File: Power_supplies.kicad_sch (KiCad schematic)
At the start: 59 parts, among them J2 DG35C-B-02P, T1 AOSP21357, T2 MJD32C, U3 MC34063, U31 AP331A, U4 MC34063, U5 TLV70233_SOT23-5

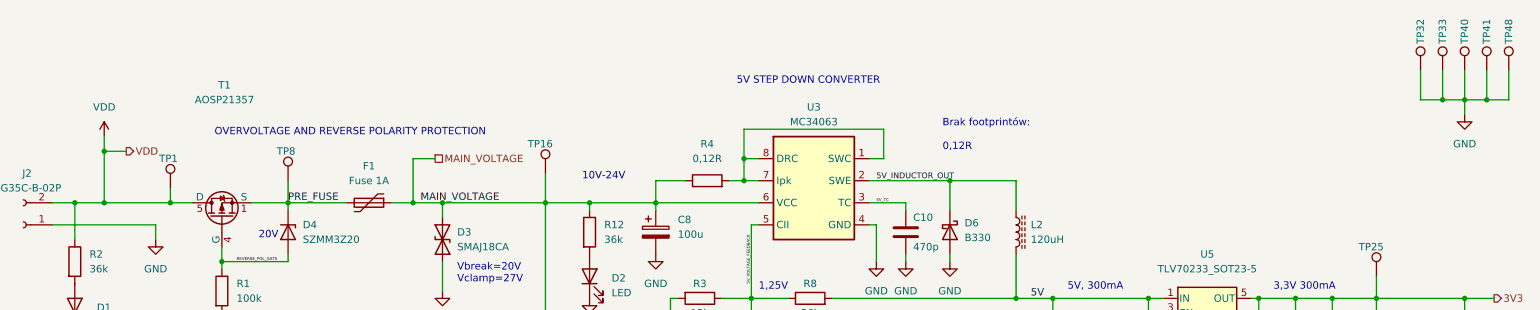
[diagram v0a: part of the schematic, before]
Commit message: moving testpoints and add new descriptions
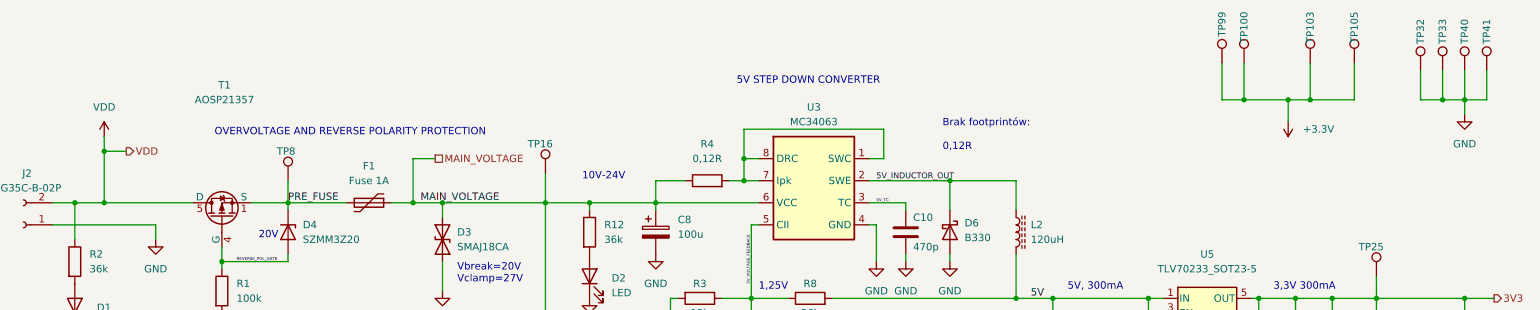
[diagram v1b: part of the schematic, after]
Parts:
- removed TP1, TP48: TestPoint, TestPoint:TestPoint_THTPad_1.0x1.0mm_Drill0.5mm, symbol Connector:TestPoint
- added TP100, TP103, TP105, TP99: TestPoint, TestPoint:TestPoint_THTPad_1.0x1.0mm_Drill0.5mm, symbol Connector:TestPoint
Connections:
- net +3V3: now also TP100.1, TP103.1, TP105.1, TP99.1
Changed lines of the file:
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@@
   (junction (at 36.83 36.83) (diameter 0) (color 0 0 0 0)
   )
+  (junction (at 245.11 27.94) (diameter 0) (color 0 0 0 0)
+  )
   (junction (at 242.57 62.23) (diameter 0) (color 0 0 0 0)
   )
@@
   (junction (at 217.17 62.23) (diameter 0) (color 0 0 0 0)
   )
+  (junction (at 233.68 27.94) (diameter 0) (color 0 0 0 0)
+  )
   (junction (at 95.25 45.72) (diameter 0) (color 0 0 0 0)
   )
+  (junction (at 241.3 27.94) (diameter 0) (color 0 0 0 0)
+  )
   (junction (at 194.31 62.23) (diameter 0) (color 0 0 0 0)
   )
@@
   (junction (at 68.58 45.72) (diameter 0) (color 0 0 0 0)
   )
-  (junction (at 48.26 45.72) (diameter 0) (color 0 0 0 0)
-  )
   (junction (at 78.74 157.48) (diameter 0) (color 0 0 0 0)
   )
@@
   (junction (at 135.89 120.65) (diameter 0) (color 0 0 0 0)
   )
-  (junction (at 275.59 27.94) (diameter 0) (color 0 0 0 0)
-  )
   (junction (at 256.54 104.14) (diameter 0) (color 0 0 0 0)
   )
@@
     (stroke (width 0) (type default) (color 0 0 0 0))
   )
-  (wire (pts (xy 36.83 45.72) (xy 48.26 45.72))
-    (stroke (width 0) (type default) (color 0 0 0 0))
-  )
   (wire (pts (xy 49.53 138.43) (xy 49.53 139.7))
     (stroke (width 0) (type default) (color 0 0 0 0))
@@
     (stroke (width 0) (type default) (color 0 0 0 0))
   )
+  (wire (pts (xy 233.68 27.94) (xy 241.3 27.94))
+    (stroke (width 0) (type default) (color 0 0 0 0))
+  )
   (wire (pts (xy 256.54 100.33) (xy 256.54 104.14))
     (stroke (width 0) (type default) (color 0 0 0 0))
@@
     (stroke (width 0) (type default) (color 0 0 0 0))
   )
-  (wire (pts (xy 279.4 27.94) (xy 279.4 22.86))
-    (stroke (width 0) (type default) (color 0 0 0 0))
-  )
   (wire (pts (xy 135.89 113.03) (xy 135.89 120.65))
     (stroke (width 0) (type default) (color 0 0 0 0))
@@
     (stroke (width 0) (type default) (color 0 0 0 0))
   )
+  (wire (pts (xy 233.68 21.59) (xy 233.68 27.94))
+    (stroke (width 0) (type default) (color 0 0 0 0))
+  )
   (wire (pts (xy 27.94 49.53) (xy 45.72 49.53))
     (stroke (width 0) (type default) (color 0 0 0 0))
@@
     (stroke (width 0) (type default) (color 0 0 0 0))
   )
+  (wire (pts (xy 241.3 27.94) (xy 245.11 27.94))
+    (stroke (width 0) (type default) (color 0 0 0 0))
+  )
+  (wire (pts (xy 252.73 27.94) (xy 252.73 21.59))
+    (stroke (width 0) (type default) (color 0 0 0 0))
+  )
   (wire (pts (xy 161.29 133.35) (xy 135.89 133.35))
     (stroke (width 0) (type default) (color 0 0 0 0))
@@
     (stroke (width 0) (type default) (color 0 0 0 0))
   )
+  (wire (pts (xy 229.87 27.94) (xy 233.68 27.94))
+    (stroke (width 0) (type default) (color 0 0 0 0))
+  )
   (wire (pts (xy 256.54 104.14) (xy 256.54 107.95))
     (stroke (width 0) (type default) (color 0 0 0 0))
@@
     (stroke (width 0) (type default) (color 0 0 0 0))
   )
-  (wire (pts (xy 275.59 27.94) (xy 279.4 27.94))
-    (stroke (width 0) (type default) (color 0 0 0 0))
-  )
   (wire (pts (xy 120.65 45.72) (xy 120.65 46.99))
     (stroke (width 0) (type default) (color 0 0 0 0))
   )
+  (wire (pts (xy 229.87 21.59) (xy 229.87 27.94))
+    (stroke (width 0) (type default) (color 0 0 0 0))
+  )
+  (wire (pts (xy 245.11 21.59) (xy 245.11 27.94))
+    (stroke (width 0) (type default) (color 0 0 0 0))
+  )
   (wire (pts (xy 135.89 133.35) (xy 130.81 133.35))
     (stroke (width 0) (type default) (color 0 0 0 0))
@@
     (stroke (width 0) (type default) (color 0 0 0 0))
   )
+  (wire (pts (xy 245.11 27.94) (xy 252.73 27.94))
+    (stroke (width 0) (type default) (color 0 0 0 0))
+  )
   (wire (pts (xy 76.2 144.78) (xy 76.2 147.32))
     (stroke (width 0) (type default) (color 0 0 0 0))
@@
     (stroke (width 0) (type default) (color 0 0 0 0))
   )
+  (wire (pts (xy 241.3 27.94) (xy 241.3 31.75))
+    (stroke (width 0) (type default) (color 0 0 0 0))
+  )
   (wire (pts (xy 143.51 62.23) (xy 148.59 62.23))
     (stroke (width 0) (type default) (color 0 0 0 0))
@@
     (stroke (width 0) (type default) (color 0 0 0 0))
   )
-  (wire (pts (xy 48.26 43.18) (xy 48.26 45.72))
-    (stroke (width 0) (type default) (color 0 0 0 0))
-  )
   (wire (pts (xy 168.91 41.91) (xy 182.88 41.91))
     (stroke (width 0) (type default) (color 0 0 0 0))
@@
     (stroke (width 0) (type default) (color 0 0 0 0))
   )
-  (wire (pts (xy 48.26 45.72) (xy 52.07 45.72))
+  (wire (pts (xy 36.83 45.72) (xy 52.07 45.72))
     (stroke (width 0) (type default) (color 0 0 0 0))
   )
@@
     (pin "1")
     (pin "2")
-  )
-  (symbol (lib_id "Connector:TestPoint") (at 48.26 43.18 0) (unit 1)
-    (in_bom yes) (on_board yes)
-    (property "Reference" "TP1" (id 0) (at 49.53 38.1 0)
-      (effects (font (size 1.27 1.27)) (justify right))
-    )
-    (property "Value" "TestPoint" (id 1) (at 45.72 38.6081 0)
-      (effects (font (size 1.27 1.27)) (justify right) hide)
-    )
-    (property "Footprint" "TestPoint:TestPoint_THTPad_1.0x1.0mm_Drill0.5mm" (id 2) (at 53.34 43.18 0)
-      (effects (font (size 1.27 1.27)) hide)
-    )
-    (property "Datasheet" "~" (id 3) (at 53.34 43.18 0)
-      (effects (font (size 1.27 1.27)) hide)
-    )
-    (pin "1")
   )
   (symbol (lib_id "Connector:TestPoint") (at 148.59 66.04 180) (unit 1)
@@
     (pin "2")
   )
+  (symbol (lib_id "power:+3.3V") (at 241.3 31.75 180) (unit 1)
+    (in_bom yes) (on_board yes) (fields_autoplaced)
+    (property "Reference" "#PWR029" (id 0) (at 241.3 27.94 0)
+      (effects (font (size 1.27 1.27)) hide)
+    )
+    (property "Value" "+3.3V" (id 1) (at 243.84 33.0199 0)
+      (effects (font (size 1.27 1.27)) (justify right))
+    )
+    (property "Footprint" "" (id 2) (at 241.3 31.75 0)
+      (effects (font (size 1.27 1.27)) hide)
+    )
+    (property "Datasheet" "" (id 3) (at 241.3 31.75 0)
+      (effects (font (size 1.27 1.27)) hide)
+    )
+    (pin "1")
+  )
   (symbol (lib_id "Connector:TestPoint") (at 275.59 22.86 0) (unit 1)
     (in_bom yes) (on_board yes)
@@
     )
     (property "Datasheet" "~" (id 3) (at 280.67 22.86 0)
+      (effects (font (size 1.27 1.27)) hide)
+    )
+    (pin "1")
+  )
+  (symbol (lib_id "Connector:TestPoint") (at 229.87 21.59 0) (unit 1)
+    (in_bom yes) (on_board yes)
+    (property "Reference" "TP99" (id 0) (at 229.87 12.7 90)
+      (effects (font (size 1.27 1.27)) (justify right))
+    )
+    (property "Value" "TestPoint" (id 1) (at 227.33 17.0181 0)
+      (effects (font (size 1.27 1.27)) (justify right) hide)
+    )
+    (property "Footprint" "TestPoint:TestPoint_THTPad_1.0x1.0mm_Drill0.5mm" (id 2) (at 234.95 21.59 0)
+      (effects (font (size 1.27 1.27)) hide)
+    )
+    (property "Datasheet" "~" (id 3) (at 234.95 21.59 0)
       (effects (font (size 1.27 1.27)) hide)
     )
@@
     (pin "1")
   )
-  (symbol (lib_id "Connector:TestPoint") (at 279.4 22.86 0) (unit 1)
-    (in_bom yes) (on_board yes)
-    (property "Reference" "TP48" (id 0) (at 279.4 13.97 90)
-      (effects (font (size 1.27 1.27)) (justify right))
-    )
-    (property "Value" "TestPoint" (id 1) (at 276.86 18.2881 0)
-      (effects (font (size 1.27 1.27)) (justify right) hide)
-    )
-    (property "Footprint" "TestPoint:TestPoint_THTPad_1.0x1.0mm_Drill0.5mm" (id 2) (at 284.48 22.86 0)
-      (effects (font (size 1.27 1.27)) hide)
-    )
-    (property "Datasheet" "~" (id 3) (at 284.48 22.86 0)
-      (effects (font (size 1.27 1.27)) hide)
-    )
-    (pin "1")
-  )
   (symbol (lib_id "power:GND") (at 271.78 81.28 0) (unit 1)
     (in_bom yes) (on_board yes) (fields_autoplaced)
@@
     (pin "1")
     (pin "2")
+  )
+  (symbol (lib_id "Connector:TestPoint") (at 233.68 21.59 0) (unit 1)
+    (in_bom yes) (on_board yes)
+    (property "Reference" "TP100" (id 0) (at 233.68 12.7 90)
+      (effects (font (size 1.27 1.27)) (justify right))
+    )
+    (property "Value" "TestPoint" (id 1) (at 231.14 17.0181 0)
+      (effects (font (size 1.27 1.27)) (justify right) hide)
+    )
+    (property "Footprint" "TestPoint:TestPoint_THTPad_1.0x1.0mm_Drill0.5mm" (id 2) (at 238.76 21.59 0)
+      (effects (font (size 1.27 1.27)) hide)
+    )
+    (property "Datasheet" "~" (id 3) (at 238.76 21.59 0)
+      (effects (font (size 1.27 1.27)) hide)
+    )
+    (pin "1")
   )
   (symbol (lib_id "Device:C_Polarized") (at 248.92 69.85 0) (unit 1)
@@
     (pin "4")
     (pin "5")
+  )
+  (symbol (lib_id "Connector:TestPoint") (at 245.11 21.59 0) (unit 1)
+    (in_bom yes) (on_board yes)
+    (property "Reference" "TP103" (id 0) (at 245.11 12.7 90)
+      (effects (font (size 1.27 1.27)) (justify right))
+    )
+    (property "Value" "TestPoint" (id 1) (at 242.57 17.0181 0)
+      (effects (font (size 1.27 1.27)) (justify right) hide)
+    )
+    (property "Footprint" "TestPoint:TestPoint_THTPad_1.0x1.0mm_Drill0.5mm" (id 2) (at 250.19 21.59 0)
+      (effects (font (size 1.27 1.27)) hide)
+    )
+    (property "Datasheet" "~" (id 3) (at 250.19 21.59 0)
+      (effects (font (size 1.27 1.27)) hide)
+    )
+    (pin "1")
   )
   (symbol (lib_id "power:GND") (at 134.62 77.47 0) (unit 1)
@@
     (pin "2")
   )
+  (symbol (lib_id "Connector:TestPoint") (at 252.73 21.59 0) (unit 1)
+    (in_bom yes) (on_board yes)
+    (property "Reference" "TP105" (id 0) (at 252.73 12.7 90)
+      (effects (font (size 1.27 1.27)) (justify right))
+    )
+    (property "Value" "TestPoint" (id 1) (at 250.19 17.0181 0)
+      (effects (font (size 1.27 1.27)) (justify right) hide)
+    )
+    (property "Footprint" "TestPoint:TestPoint_THTPad_1.0x1.0mm_Drill0.5mm" (id 2) (at 257.81 21.59 0)
+      (effects (font (size 1.27 1.27)) hide)
+    )
+    (property "Datasheet" "~" (id 3) (at 257.81 21.59 0)
+      (effects (font (size 1.27 1.27)) hide)
+    )
+    (pin "1")
+  )
   (symbol (lib_id "Diode:B330") (at 182.88 50.8 270) (unit 1)
